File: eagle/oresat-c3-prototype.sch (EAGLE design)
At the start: 108 parts, among them J1 J-SAMTEC-TFM-110-X1-XXX-D-RA, J10 2X8X1.27, J11 2X8X1.27, J12 2X8X1.27, J2 U.FL, J3 U.FL, J4 U.FL, J6 J-SAMTEC-TFM-120-X1-XXX-D-RA, J7 FTSH-105-XX-X-DV-K, J8 SD_CARD_SOCKET, J9 2X8X1.27, Q1 MOSFET-PCH-SOT23-6, Q2 MOSFET-PCH-SOT23-6, U1 MAX892LEUA+T, U2 TCAN330, U3 TCAN330, U4 TPS259621 - eFuse, U5 TPS62111RSA, U6 MAX6373KA+21-0078H-L, U7 STM32F446RE, X1 16MHZ-2.5x2mm

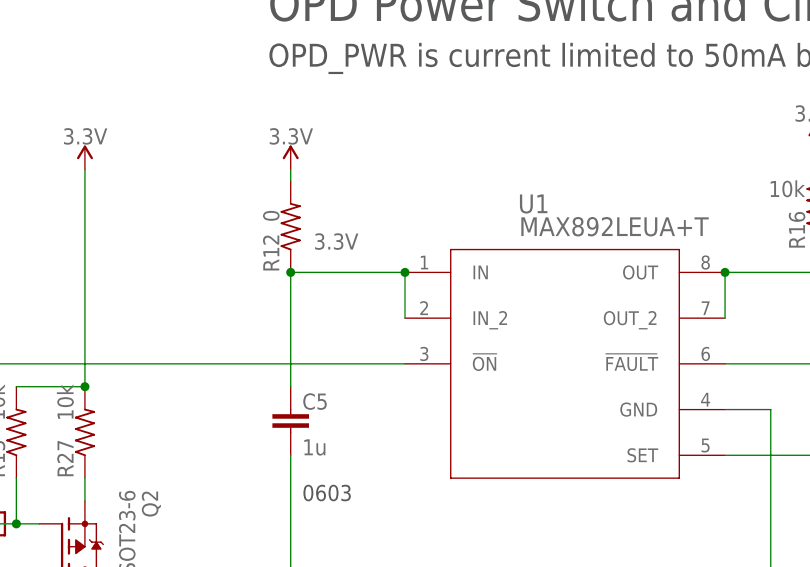
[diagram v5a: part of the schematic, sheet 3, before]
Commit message: Fixed some erc errors
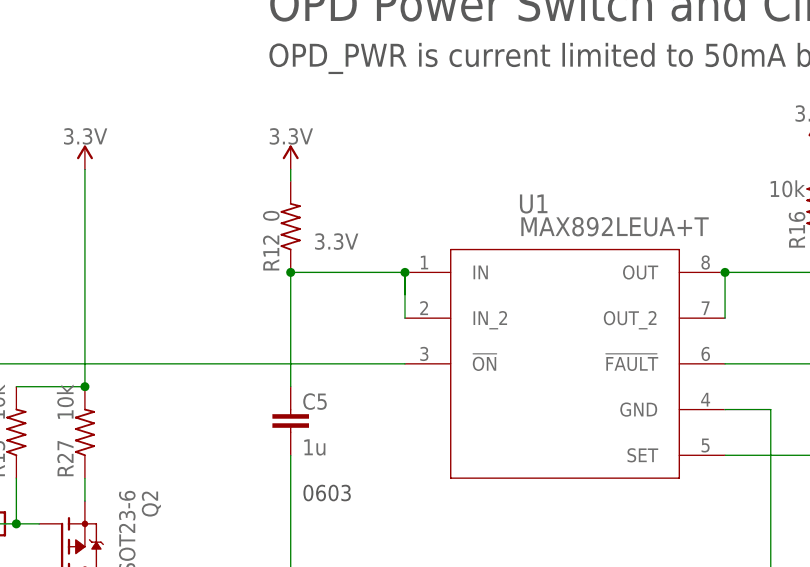
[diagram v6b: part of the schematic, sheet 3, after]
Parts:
- D7: value (none) -> 1N4148
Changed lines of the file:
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@@
 <part name="R13" library="rcl" library_urn="urn:adsk.eagle:library:334" deviceset="R-US_" device="R0402" package3d_urn="urn:adsk.eagle:package:23547/2" value="4.7k"/>
 <part name="SUPPLY15" library="SparkFun-PowerSymbols" library_urn="urn:adsk.eagle:library:530" deviceset="3.3V" device=""/>
-<part name="U4" library="Robins_Parts" deviceset="TPS2596XX" device="" value="TPS259621 - eFuse"/>
 <part name="Q2" library="Q-MOSFET-PCH-SOT23-6" deviceset="MOSFET-PCH-SOT23-6" device="">
 <attribute name="MFR" value="Diodes Inc"/>
@@
 </part>
 <part name="GND32" library="supply1" library_urn="urn:adsk.eagle:library:371" deviceset="GND" device=""/>
-<part name="U1" library="Robins_Parts" deviceset="MAX892LEUA+T" device=""/>
 <part name="JP4" library="pinhead" library_urn="urn:adsk.eagle:library:325" deviceset="PINHD-1X10" device="" package3d_urn="urn:adsk.eagle:package:22406/2"/>
 <part name="J9" library="2x8x1.27" deviceset="2X8X1.27" device=""/>
@@
 <part name="TP7" library="Tova" deviceset="TEST-POINT" device=""/>
 <part name="TP11" library="Tova" deviceset="TEST-POINT" device=""/>
-<part name="D7" library="SparkFun" deviceset="DIODE" device="SOD"/>
+<part name="D7" library="SparkFun" deviceset="DIODE" device="SOD" value="1N4148"/>
+<part name="U4" library="Robins_Parts" deviceset="TPS2596XX" device="" value="TPS259621 - eFuse"/>
+<part name="U1" library="Robins_Parts" deviceset="MAX892LEUA+T" device=""/>
 </parts>
 <sheets>
@@
 <attribute name="VALUE" x="124.46" y="185.42" size="1.778" layer="96" rot="MR0"/>
 </instance>
+<instance part="TP1" gate="G$1" x="116.84" y="210.82" smashed="yes">
+<attribute name="NAME" x="114.3" y="207.01" size="1.778" layer="95" font="vector"/>
+</instance>
 <instance part="U4" gate="G$1" x="96.52" y="208.28" smashed="yes">
 <attribute name="NAME" x="88.9" y="223.52" size="1.778" layer="95"/>
 <attribute name="VALUE" x="88.9" y="220.98" size="1.778" layer="96"/>
-</instance>
-<instance part="TP1" gate="G$1" x="116.84" y="210.82" smashed="yes">
-<attribute name="NAME" x="114.3" y="207.01" size="1.778" layer="95" font="vector"/>
 </instance>
 </instances>
@@
 <pinref part="R6" gate="R" pin="2"/>
 <pinref part="TP10" gate="G$1" pin="1"/>
-<pinref part="U4" gate="G$1" pin="ILIM"/>
 <wire x1="111.76" y1="205.74" x2="121.92" y2="205.74" width="0.1524" layer="91"/>
 <junction x="121.92" y="205.74"/>
@@
 <wire x1="134.62" y1="210.82" x2="170.18" y2="210.82" width="0.1524" layer="91"/>
 <label x="170.18" y="210.82" size="1.778" layer="95" xref="yes"/>
+<pinref part="U4" gate="G$1" pin="ILIM"/>
 </segment>
 </net>
@@
 <net name="!CB_FLT" class="0">
 <segment>
-<pinref part="U4" gate="G$1" pin="!FLT"/>
 <pinref part="TP1" gate="G$1" pin="1"/>
 <wire x1="111.76" y1="210.82" x2="116.84" y2="210.82" width="0.1524" layer="91"/>
+<pinref part="U4" gate="G$1" pin="!FLT"/>
 </segment>
 </net>
@@
 <attribute name="VALUE" x="215.9" y="142.24" size="1.778" layer="96" rot="MR0"/>
 </instance>
-<instance part="U1" gate="A" x="180.34" y="175.26" smashed="yes">
-<attribute name="NAME" x="175.1076" y="189.4586" size="2.0828" layer="95" ratio="6" rot="SR0"/>
-<attribute name="VALUE" x="175.2346" y="186.9186" size="2.0828" layer="96" ratio="6" rot="SR0"/>
-</instance>
 <instance part="SUPPLY4" gate="G$1" x="149.86" y="194.31" smashed="yes">
 <attribute name="VALUE" x="149.86" y="197.104" size="1.778" layer="96" align="bottom-center"/>
@@
 <attribute name="VALUE" x="208.28" y="199.644" size="1.778" layer="96" align="bottom-center"/>
 </instance>
+<instance part="U1" gate="A" x="180.34" y="175.26" smashed="yes">
+<attribute name="NAME" x="175.1076" y="189.4586" size="2.0828" layer="95" ratio="6" rot="SR0"/>
+<attribute name="VALUE" x="175.2346" y="186.9186" size="2.0828" layer="96" ratio="6" rot="SR0"/>
+</instance>
 </instances>
 <busses>
@@
 <pinref part="GND23" gate="1" pin="GND"/>
 <wire x1="203.2" y1="147.32" x2="203.2" y2="167.64" width="0.1524" layer="91"/>
+<wire x1="203.2" y1="167.64" x2="198.12" y2="167.64" width="0.1524" layer="91"/>
 <pinref part="U1" gate="A" pin="GND"/>
-<wire x1="203.2" y1="167.64" x2="198.12" y2="167.64" width="0.1524" layer="91"/>
 </segment>
 </net>
@@
 </segment>
 <segment>
-<pinref part="U1" gate="A" pin="IN_2"/>
-<pinref part="U1" gate="A" pin="IN"/>
-<wire x1="162.56" y1="182.88" x2="162.56" y2="177.8" width="0.1524" layer="91"/>
-<junction x="162.56" y="182.88"/>
 <pinref part="C5" gate="CE" pin="1"/>
 <wire x1="149.86" y1="182.88" x2="162.56" y2="182.88" width="0.1524" layer="91"/>
@@
 <pinref part="R12" gate="R" pin="1"/>
 <junction x="149.86" y="182.88"/>
+<wire x1="162.56" y1="182.88" x2="162.56" y2="180.4162" width="0.1524" layer="91"/>
+<pinref part="U1" gate="A" pin="IN"/>
+<junction x="162.56" y="182.88"/>
+<pinref part="U1" gate="A" pin="IN_2"/>
+<wire x1="162.56" y1="182.88" x2="162.56" y2="177.8" width="0.1524" layer="91"/>
 </segment>
 <segment>
@@
 <junction x="248.92" y="162.56"/>
 <pinref part="TP14" gate="G$1" pin="1"/>
-<pinref part="U1" gate="A" pin="SET"/>
 <wire x1="198.12" y1="162.56" x2="248.92" y2="162.56" width="0.1524" layer="91"/>
 <wire x1="248.92" y1="162.56" x2="271.78" y2="162.56" width="0.1524" layer="91"/>
 <label x="271.78" y="162.56" size="1.778" layer="95" xref="yes"/>
+<pinref part="U1" gate="A" pin="SET"/>
 </segment>
 </net>
@@
 <wire x1="198.12" y1="172.72" x2="208.28" y2="172.72" width="0.1524" layer="91"/>
 <wire x1="208.28" y1="172.72" x2="208.28" y2="185.42" width="0.1524" layer="91"/>
-<pinref part="U1" gate="A" pin="!FAULT"/>
 <pinref part="R16" gate="R" pin="1"/>
 <wire x1="208.28" y1="172.72" x2="223.52" y2="172.72" width="0.1524" layer="91"/>
 <junction x="208.28" y="172.72"/>
+<pinref part="U1" gate="A" pin="!FAULT"/>
 </segment>
 </net>
@@
 <pinref part="C4" gate="CE" pin="1"/>
 <junction x="213.36" y="182.88"/>
+<wire x1="198.12" y1="177.8" x2="198.12" y2="182.88" width="0.1524" layer="91"/>
+<pinref part="U1" gate="A" pin="OUT_2"/>
 <pinref part="U1" gate="A" pin="OUT"/>
-<pinref part="U1" gate="A" pin="OUT_2"/>
-<wire x1="198.12" y1="177.8" x2="198.12" y2="182.88" width="0.1524" layer="91"/>
 <junction x="198.12" y="182.88"/>
 </segment>
@@
 <label x="106.68" y="172.72" size="1.778" layer="95" rot="R180" xref="yes"/>
 <wire x1="106.68" y1="172.72" x2="114.3" y2="172.72" width="0.1524" layer="91"/>
-<pinref part="U1" gate="A" pin="!ON"/>
 <wire x1="114.3" y1="172.72" x2="162.56" y2="172.72" width="0.1524" layer="91"/>
 <wire x1="114.3" y1="172.72" x2="114.3" y2="154.94" width="0.1524" layer="91"/>
@@
 <wire x1="114.3" y1="154.94" x2="116.84" y2="154.94" width="0.1524" layer="91"/>
 <junction x="116.84" y="154.94"/>
-</segment>
-</net>
+<pinref part="U1" gate="A" pin="!ON"/>
+</segment>
+</net>

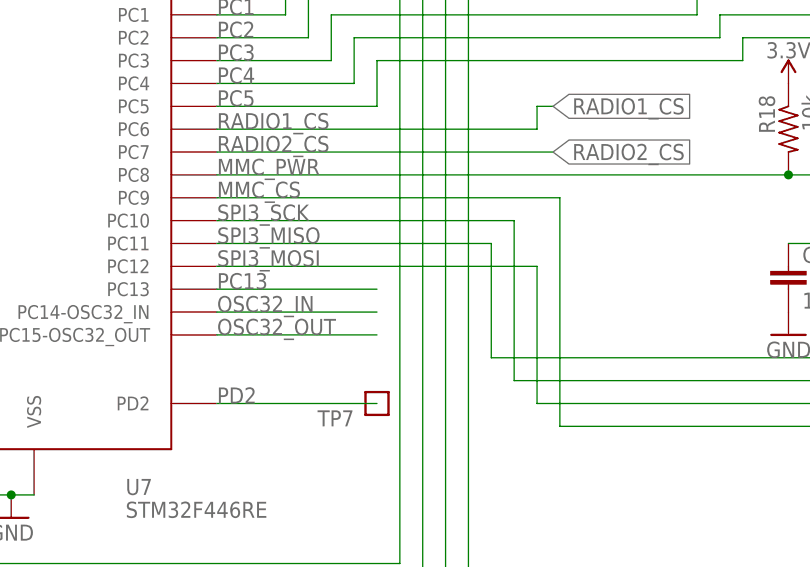
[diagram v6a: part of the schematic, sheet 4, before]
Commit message: Added TP for one last MCU pin
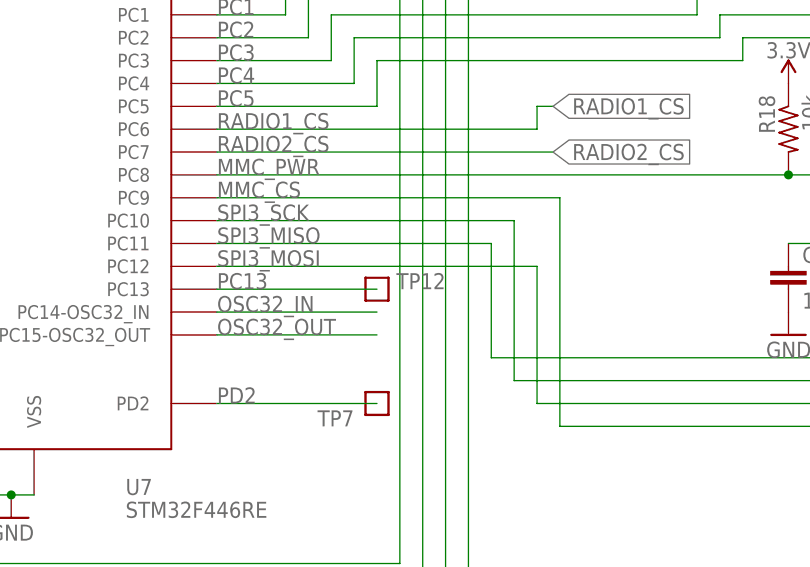
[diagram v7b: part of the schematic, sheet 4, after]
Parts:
- added TP12: TEST-POINT, Tova:TEST-POINT
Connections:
- net PC13: now also TP12.1
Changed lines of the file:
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@@
 <?xml version="1.0" encoding="utf-8"?>
 <!DOCTYPE eagle SYSTEM "eagle.dtd">
-<eagle version="9.5.1">
+<eagle version="9.5.2">
 <drawing>
 <settings>
@@
 <part name="U4" library="Robins_Parts" deviceset="TPS2596XX" device="" value="TPS259621 - eFuse"/>
 <part name="U1" library="Robins_Parts" deviceset="MAX892LEUA+T" device=""/>
+<part name="TP12" library="Tova" deviceset="TEST-POINT" device=""/>
 </parts>
 <sheets>
@@
 <pinref part="U1" gate="A" pin="OUT"/>
 <junction x="198.12" y="182.88"/>
+<label x="210.82" y="182.88" size="1.778" layer="95"/>
 </segment>
 <segment>
@@
 <attribute name="VALUE" x="383.54" y="251.2314" size="1.778" layer="96" rot="R180"/>
 </instance>
+<instance part="TP12" gate="G$1" x="254" y="81.28" smashed="yes" rot="MR0">
+<attribute name="NAME" x="261.62" y="81.28" size="1.778" layer="95" font="vector" rot="MR0"/>
+</instance>
 </instances>
 <busses>
@@
 <label x="236.22" y="81.28" size="1.778" layer="95"/>
 <pinref part="U7" gate="G$1" pin="PC13"/>
+<pinref part="TP12" gate="G$1" pin="1"/>
 </segment>
 </net>

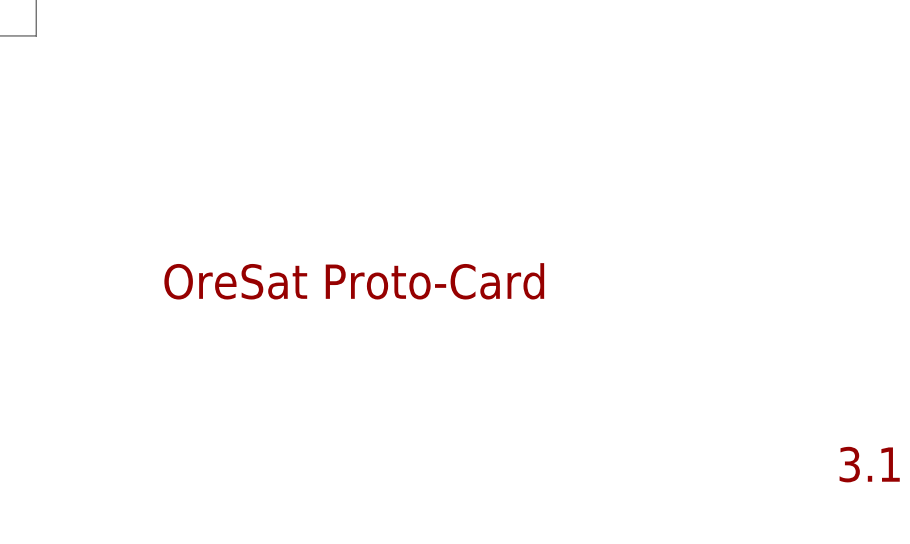
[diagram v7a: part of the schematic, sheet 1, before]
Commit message: Approved some of the ERC warnings
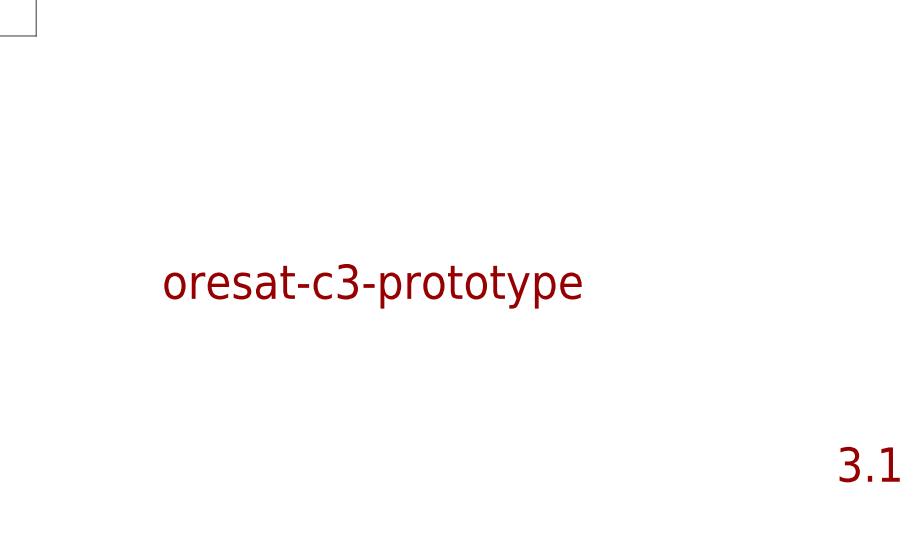
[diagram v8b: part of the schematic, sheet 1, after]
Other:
- note added: "oresat-c3-prototype"
- note removed: "OreSat Proto-Card"
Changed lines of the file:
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@@
 <description>Connectors</description>
 <plain>
-<text x="341.63" y="26.67" size="3.81" layer="94">OreSat Proto-Card</text>
+<text x="341.63" y="26.67" size="3.81" layer="94">oresat-c3-prototype</text>
 <text x="416.56" y="6.35" size="3.81" layer="94">3.1</text>
 <text x="11.43" y="5.08" size="1.778" layer="97">All resistors 0402 +/- 1% unless marked</text>
